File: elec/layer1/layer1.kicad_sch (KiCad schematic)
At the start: 124 parts, among them J1 XT30PW-M, J2 XT30PW-M, J3 Conn_01x04, J4 XT30PW-M, J5 XT30PW-M, SW2 SW_SPDT_312, U1 CD74HC4067SM, U2 CD74HC4067SM, U3 TEENSY40

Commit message: fix: l1 gnd
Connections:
- net GND: now also U3.G1, U3.G2, U3.G3
- no-connect marks 24 -> 21
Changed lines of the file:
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@@
 	(title_block
 		(title "Robocup 2026 Layer 1")
-		(date "2026-01-28")
-		(rev "0.1")
+		(date "2026-01-29")
+		(rev "1.0")
 		(company "Vent Exhaust")
 		(comment 1 "Ng Chen-Xuan")
@@
 	)
 	(no_connect
-		(at 247.65 170.18)
-	)
-	(no_connect
 		(at 247.65 198.12)
 	)
@@
 	)
 	(no_connect
-		(at 283.21 172.72)
-	)
-	(no_connect
 		(at 283.21 175.26)
 	)
@@
 	)
 	(no_connect
-		(at 247.65 213.36)
-	)
-	(no_connect
 		(at 283.21 180.34)
 	)
@@
 	(wire
 		(pts
+			(xy 234.95 170.18) (xy 247.65 170.18)
+		)
+		(stroke
+			(width 0)
+			(type default)
+		)
+	)
+	(wire
+		(pts
 			(xy 57.15 208.28) (xy 57.15 207.01)
 		)
@@
 	(wire
 		(pts
+			(xy 234.95 213.36) (xy 247.65 213.36)
+		)
+		(stroke
+			(width 0)
+			(type default)
+		)
+	)
+	(wire
+		(pts
 			(xy 146.05 31.75) (xy 146.05 33.02)
 		)
@@
 	(wire
 		(pts
+			(xy 283.21 172.72) (xy 295.91 172.72)
+		)
+		(stroke
+			(width 0)
+			(type default)
+		)
+	)
+	(wire
+		(pts
 			(xy 176.53 190.5) (xy 176.53 189.23)
 		)
@@
 	)
 	(symbol
+		(lib_id "power:GND")
+		(at 234.95 170.18 270)
+		(unit 1)
+		(exclude_from_sim no)
+		(in_bom yes)
+		(on_board yes)
+		(dnp no)
+		(fields_autoplaced yes)
+		(property "Reference" "#PWR039"
+			(at 228.6 170.18 0)
+			(effects
+				(font
+					(size 1.27 1.27)
+				)
+				(hide yes)
+			)
+		)
+		(property "Value" "GND"
+			(at 231.14 170.1799 90)
+			(effects
+				(font
+					(size 1.27 1.27)
+				)
+				(justify right)
+			)
+		)
+		(property "Footprint" ""
+			(at 234.95 170.18 0)
+			(effects
+				(font
+					(size 1.27 1.27)
+				)
+				(hide yes)
+			)
+		)
+		(property "Datasheet" ""
+			(at 234.95 170.18 0)
+			(effects
+				(font
+					(size 1.27 1.27)
+				)
+				(hide yes)
+			)
+		)
+		(property "Description" "Power symbol creates a global label with name \"GND\" , ground"
+			(at 234.95 170.18 0)
+			(effects
+				(font
+					(size 1.27 1.27)
+				)
+				(hide yes)
+			)
+		)
+		(pin "1"
+		)
+		(instances
+			(project "layer1"
+				(path "/65f958e3-40ee-4841-b9d1-28823b8d4e62"
+					(reference "#PWR039")
+					(unit 1)
+				)
+			)
+		)
+	)
+	(symbol
 		(lib_id "power:+3V3")
 		(at 135.89 246.38 0)
@@
 	)
 	(symbol
+		(lib_id "power:GND")
+		(at 295.91 172.72 90)
+		(unit 1)
+		(exclude_from_sim no)
+		(in_bom yes)
+		(on_board yes)
+		(dnp no)
+		(fields_autoplaced yes)
+		(property "Reference" "#PWR038"
+			(at 302.26 172.72 0)
+			(effects
+				(font
+					(size 1.27 1.27)
+				)
+				(hide yes)
+			)
+		)
+		(property "Value" "GND"
+			(at 299.72 172.7199 90)
+			(effects
+				(font
+					(size 1.27 1.27)
+				)
+				(justify right)
+			)
+		)
+		(property "Footprint" ""
+			(at 295.91 172.72 0)
+			(effects
+				(font
+					(size 1.27 1.27)
+				)
+				(hide yes)
+			)
+		)
+		(property "Datasheet" ""
+			(at 295.91 172.72 0)
+			(effects
+				(font
+					(size 1.27 1.27)
+				)
+				(hide yes)
+			)
+		)
+		(property "Description" "Power symbol creates a global label with name \"GND\" , ground"
+			(at 295.91 172.72 0)
+			(effects
+				(font
+					(size 1.27 1.27)
+				)
+				(hide yes)
+			)
+		)
+		(pin "1"
+		)
+		(instances
+			(project ""
+				(path "/65f958e3-40ee-4841-b9d1-28823b8d4e62"
+					(reference "#PWR038")
+					(unit 1)
+				)
+			)
+		)
+	)
+	(symbol
 		(lib_id "Device:LED")
 		(at 259.08 36.83 90)
@@
 					(unit 1)
 				)
+			)
+		)
+	)
+	(symbol
+		(lib_id "power:GND")
+		(at 234.95 213.36 270)
+		(unit 1)
+		(exclude_from_sim no)
+		(in_bom yes)
+		(on_board yes)
+		(dnp no)
+		(fields_autoplaced yes)
+		(property "Reference" "#PWR040"
+			(at 228.6 213.36 0)
+			(effects
+				(font
+					(size 1.27 1.27)
+				)
+				(hide yes)
+			)
+		)
+		(property "Value" "GND"
+			(at 231.14 213.3599 90)
+			(effects
+				(font
+					(size 1.27 1.27)
+				)
+				(justify right)
+			)
+		)
+		(property "Footprint" ""
+			(at 234.95 213.36 0)
+			(effects
+				(font
+					(size 1.27 1.27)
+				)
+				(hide yes)
+			)
+		)
+		(property "Datasheet" ""
+			(at 234.95 213.36 0)
+			(effects
+				(font
+					(size 1.27 1.27)
+				)
+				(hide yes)
+			)
+		)
+		(property "Description" "Power symbol creates a global label with name \"GND\" , ground"
+			(at 234.95 213.36 0)
+			(effects
+				(font
+					(size 1.27 1.27)
+				)
+				(hide yes)
+			)
+		)
+		(pin "1"
+		)
+		(instances
+			(project "layer1"
+				(path "/65f958e3-40ee-4841-b9d1-28823b8d4e62"
+					(reference "#PWR040")
+					(unit 1)
+				)

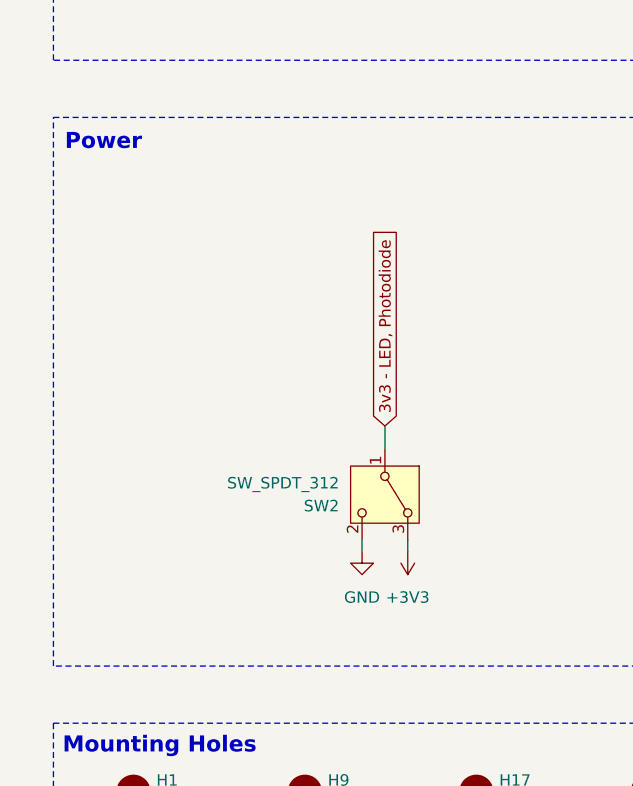
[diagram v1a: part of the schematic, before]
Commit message: changed chenxuan mistake on l1
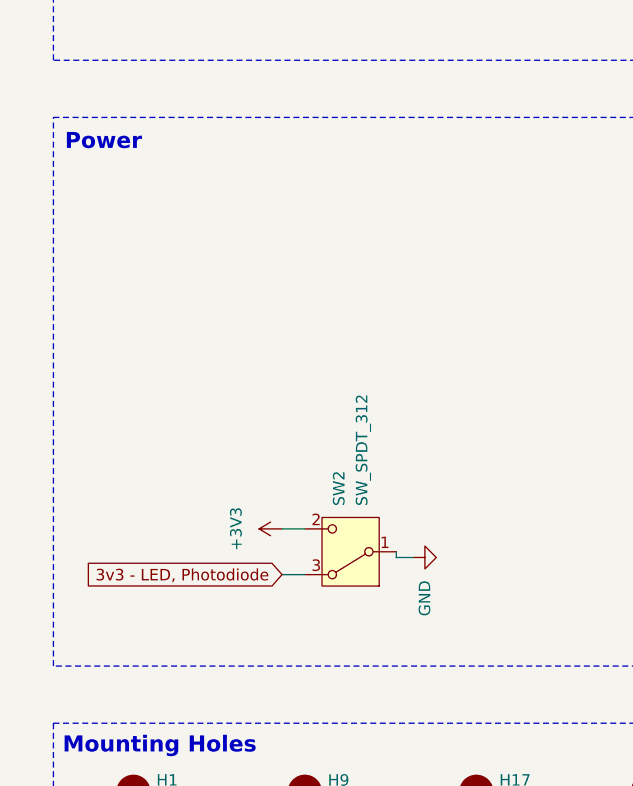
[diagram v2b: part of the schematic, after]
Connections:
- net +3V3: now also SW2.2 (C); no longer SW2.3 (A)
- net 3v3 - LED, Photodiode: now also SW2.3 (A); no longer SW2.1 (B)
- net GND: now also SW2.1 (B); no longer SW2.2 (C)
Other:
- moved on the sheet: SW2
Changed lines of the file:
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@@
 	(wire
 		(pts
+			(xy 55.88 208.915) (xy 57.785 208.915)
+		)
+		(stroke
+			(width 0)
+			(type default)
+		)
+	)
+	(wire
+		(pts
 			(xy 170.18 87.63) (xy 172.72 87.63)
 		)
@@
 	(wire
 		(pts
+			(xy 43.18 210.82) (xy 45.72 210.82)
+		)
+		(stroke
+			(width 0)
+			(type default)
+		)
+	)
+	(wire
+		(pts
 			(xy 95.25 31.75) (xy 105.41 31.75)
 		)
@@
 	(wire
 		(pts
-			(xy 57.15 208.28) (xy 57.15 207.01)
-		)
-		(stroke
-			(width 0)
-			(type default)
-		)
-	)
-	(wire
-		(pts
 			(xy 81.28 87.63) (xy 83.82 87.63)
 		)
@@
 	(wire
 		(pts
+			(xy 43.18 205.74) (xy 45.72 205.74)
+		)
+		(stroke
+			(width 0)
+			(type default)
+		)
+	)
+	(wire
+		(pts
 			(xy 135.89 40.64) (xy 135.89 41.91)
 		)
@@
 	(wire
 		(pts
+			(xy 55.88 208.28) (xy 55.88 208.915)
+		)
+		(stroke
+			(width 0)
+			(type default)
+		)
+	)
+	(wire
+		(pts
 			(xy 340.36 41.91) (xy 330.2 41.91)
 		)
@@
 	(wire
 		(pts
-			(xy 54.61 194.31) (xy 54.61 196.85)
-		)
-		(stroke
-			(width 0)
-			(type default)
-		)
-	)
-	(wire
-		(pts
 			(xy 160.02 123.19) (xy 160.02 124.46)
 		)
@@
 	(wire
 		(pts
-			(xy 52.07 208.28) (xy 52.07 207.01)
-		)
-		(stroke
-			(width 0)
-			(type default)
-		)
-	)
-	(wire
-		(pts
 			(xy 185.42 187.96) (xy 185.42 189.23)
 		)
@@
 	(global_label "3v3 - LED, Photodiode"
 		(shape input)
-		(at 54.61 194.31 90)
+		(at 43.18 210.82 180)
 		(fields_autoplaced yes)
 		(effects
@@
 				(size 1.27 1.27)
 			)
-			(justify left)
+			(justify right)
 		)
 		(property "Intersheetrefs" "${INTERSHEET_REFS}"
-			(at 54.61 168.828 90)
+			(at 17.698 210.82 0)
 			(effects
 				(font
 					(size 1.27 1.27)
 				)
-				(justify left)
+				(justify right)
 				(hide yes)
 			)
@@
 	(symbol
 		(lib_id "power:GND")
-		(at 52.07 208.28 0)
+		(at 57.785 208.915 90)
 		(unit 1)
 		(exclude_from_sim no)
@@
 		(fields_autoplaced yes)
 		(property "Reference" "#PWR027"
-			(at 52.07 214.63 0)
+			(at 64.135 208.915 0)
 			(effects
 				(font
@@
 		)
 		(property "Value" "GND"
-			(at 52.07 213.36 0)
+			(at 59.0551 211.455 0)
 			(effects
 				(font
 					(size 1.27 1.27)
 				)
+				(justify right)
 			)
 		)
 		(property "Footprint" ""
-			(at 52.07 208.28 0)
+			(at 57.785 208.915 0)
 			(effects
 				(font
@@
 		)
 		(property "Datasheet" ""
-			(at 52.07 208.28 0)
+			(at 57.785 208.915 0)
 			(effects
 				(font
@@
 		)
 		(property "Description" "Power symbol creates a global label with name \"GND\" , ground"
-			(at 52.07 208.28 0)
+			(at 57.785 208.915 0)
 			(effects
 				(font
@@
 	(symbol
 		(lib_id "Switch:SW_SPDT_312")
-		(at 54.61 201.93 270)
+		(at 50.8 208.28 180)
 		(unit 1)
 		(exclude_from_sim no)
@@
 		(fields_autoplaced yes)
 		(property "Reference" "SW2"
-			(at 49.53 203.2001 90)
+			(at 49.5299 203.2 90)
 			(effects
 				(font
@@
 		)
 		(property "Value" "SW_SPDT_312"
-			(at 49.53 200.6601 90)
+			(at 52.0699 203.2 90)
 			(effects
 				(font
@@
 		)
 		(property "Footprint" "layer1-pcb-footprints:SS12D00G3"
-			(at 44.45 201.93 0)
+			(at 50.8 198.12 0)
 			(effects
 				(font
@@
 		)
 		(property "Datasheet" "~"
-			(at 46.99 201.93 0)
+			(at 50.8 200.66 0)
 			(effects
 				(font
@@
 		)
 		(property "Description" "Switch, single pole double throw"
-			(at 54.61 201.93 0)
+			(at 50.8 208.28 0)
 			(effects
 				(font
@@
 	(symbol
 		(lib_id "power:+3V3")
-		(at 57.15 208.28 180)
+		(at 43.18 205.74 90)
 		(unit 1)
 		(exclude_from_sim no)
@@
 		(fields_autoplaced yes)
 		(property "Reference" "#PWR01"
-			(at 57.15 204.47 0)
+			(at 46.99 205.74 0)
 			(effects
 				(font
@@
 		)
 		(property "Value" "+3V3"
-			(at 57.15 213.36 0)
+			(at 38.1 205.74 0)
 			(effects
 				(font
@@
 		)
 		(property "Footprint" ""
-			(at 57.15 208.28 0)
+			(at 43.18 205.74 0)
 			(effects
 				(font
@@
 		)
 		(property "Datasheet" ""
-			(at 57.15 208.28 0)
+			(at 43.18 205.74 0)
 			(effects
 				(font
@@
 		)
 		(property "Description" "Power symbol creates a global label with name \"+3V3\""
-			(at 57.15 208.28 0)
+			(at 43.18 205.74 0)
 			(effects
 				(font

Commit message: did l1 add res partially
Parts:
- added C5, C6: 220u, Capacitor_Tantalum_SMD:CP_EIA-7343-15_Kemet-W_HandSolder, symbol Device:C_Polarized
- added R10, R11, R12, R13, R14, R15, R16, R17, R18, R19, R20, R21, R22, R23, R24, R25, R26, R27, R28, R29, R30, R31, R32, R33, R34, R35, R36, R5, R6, R7, R8, R9: 0R39, Resistor_SMD:R_0603_1608Metric, symbol Device:R
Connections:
- net +3V3: now also C5.1, C6.1
- net 3v3 - LED, Photodiode: now also R10.1, R11.1, R12.1, R13.1, R14.1, R15.1, R16.1, R17.1, R18.1, R19.1, R20.1, R21.1, R22.1, R23.1, R24.1, R25.1, R26.1, R27.1, R28.1, R29.1, R30.1, R31.1, R32.1, R33.1, R34.1, R35.1, R36.1, R5.1, R6.1, R7.1, R8.1, R9.1; no longer D1.2 (A), D10.2 (A), D11.2 (A), D12.2 (A), D13.2 (A), D14.2 (A), D15.2 (A), D16.2 (A), D17.2 (A), D18.2 (A), D19.2 (A), D2.2 (A), D20.2 (A), D21.2 (A), D22.2 (A), D23.2 (A), D24.2 (A), D25.2 (A), D26.2 (A), D27.2 (A), D28.2 (A), D29.2 (A), D3.2 (A), D30.2 (A), D31.2 (A), D32.2 (A), D4.2 (A), D5.2 (A), D6.2 (A), D7.2 (A), D8.2 (A), D9.2 (A)
- net GND: now also C5.2, C6.2
- new net: D30.2 (A), R34.2
- new net: D14.2 (A), R18.2
- new net: D29.2 (A), R33.2
- new net: D12.2 (A), R16.2
- new net: D17.2 (A), R21.2
- new net: D13.2 (A), R17.2
- new net: D26.2 (A), R30.2
- new net: D10.2 (A), R14.2
- new net: D23.2 (A), R27.2
- new net: D5.2 (A), R9.2
- new net: D19.2 (A), R23.2
- new net: D20.2 (A), R24.2
- new net: D15.2 (A), R19.2
- new net: D9.2 (A), R13.2
- new net: D24.2 (A), R28.2
- new net: D7.2 (A), R11.2
- new net: D1.2 (A), R5.2
- new net: D8.2 (A), R12.2
- new net: D3.2 (A), R7.2
- new net: D4.2 (A), R8.2
- new net: D21.2 (A), R25.2
- new net: D18.2 (A), R22.2
- new net: D22.2 (A), R26.2
- new net: D32.2 (A), R36.2
- new net: D31.2 (A), R35.2
- new net: D6.2 (A), R10.2
- new net: D16.2 (A), R20.2
- new net: D25.2 (A), R29.2
- new net: D2.2 (A), R6.2
- new net: D11.2 (A), R15.2
- new net: D27.2 (A), R31.2
- new net: D28.2 (A), R32.2
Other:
- moved on the sheet: D1, D10, D11, D12, D13, D14, D15, D16, D17, D18, D19, D2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

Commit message: fix: l1; prod: l1
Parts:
- H1, H2: footprint MountingHole:MountingHole_2.2mm_M2_DIN965_Pad_TopBottom -> MountingHole:MountingHole_3.2mm_M3_DIN965_Pad_TopBottom
- R10, R11, R12, R13, R14, R15, R16, R17, R18, R19, R20, R21, R22, R23, R24, R25, R26, R27, R28, R29, R30, R31, R32, R33, R34, R35, R36, R5, R6, R7, R8, R9: value 0R39 -> 10R
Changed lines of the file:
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@@
 	(wire
 		(pts
-			(xy 43.18 27.94) (xy 76.2 27.94)
+			(xy 63.5 27.94) (xy 76.2 27.94)
 		)
 		(stroke
@@
 	(wire
 		(pts
-			(xy 43.18 27.94) (xy 43.18 25.4)
-		)
-		(stroke
-			(width 0)
-			(type default)
-		)
-	)
-	(wire
-		(pts
 			(xy 60.96 96.52) (xy 60.96 97.79)
 		)
@@
 	(global_label "3v3 - LED, Photodiode"
 		(shape input)
-		(at 43.18 25.4 180)
+		(at 63.5 27.94 180)
 		(fields_autoplaced yes)
 		(effects
@@
 		)
 		(property "Intersheetrefs" "${INTERSHEET_REFS}"
-			(at 17.698 25.4 0)
+			(at 38.018 27.94 0)
 			(effects
 				(font
@@
 			)
 		)
-		(property "Value" "0R39"
+		(property "Value" "10R"
 			(at 374.65 34.2899 0)
 			(effects
@@
 			)
 		)
-		(property "Value" "0R39"
+		(property "Value" "10R"
 			(at 210.82 34.2899 0)
 			(effects
@@
 			)
 		)
-		(property "Value" "0R39"
+		(property "Value" "10R"
 			(at 334.01 34.2899 0)
 			(effects
@@
 			)
 		)
-		(property "Value" "0R39"
+		(property "Value" "10R"
 			(at 190.5 34.2899 0)
 			(effects
@@
 			)
 		)
-		(property "Value" "0R39"
+		(property "Value" "10R"
 			(at 170.18 34.2899 0)
 			(effects
@@
 			)
 		)
-		(property "Value" "0R39"
+		(property "Value" "10R"
 			(at 303.53 34.2899 0)
 			(effects
@@
 			)
 		)
-		(property "Value" "0R39"
+		(property "Value" "10R"
 			(at 119.38 34.2899 0)
 			(effects
@@
 			)
 		)
-		(property "Value" "0R39"
+		(property "Value" "10R"
 			(at 200.66 34.2899 0)
 			(effects
@@
 			)
 		)
-		(property "Value" "0R39"
+		(property "Value" "10R"
 			(at 364.49 34.2899 0)
 			(effects
@@
 			)
 		)
-		(property "Value" "0R39"
+		(property "Value" "10R"
 			(at 220.98 34.2899 0)
 			(effects
@@
 			)
 		)
-		(property "Footprint" "MountingHole:MountingHole_2.2mm_M2_DIN965_Pad_TopBottom"
+		(property "Footprint" "MountingHole:MountingHole_3.2mm_M3_DIN965_Pad_TopBottom"
 			(at 26.67 240.03 0)
 			(effects
@@
 			)
 		)
-		(property "Value" "0R39"
+		(property "Value" "10R"
 			(at 313.69 34.2899 0)
 			(effects
@@
 			)
 		)
-		(property "Value" "0R39"
+		(property "Value" "10R"
 			(at 139.7 34.2899 0)
 			(effects
@@
 			)
 		)
-		(property "Footprint" "MountingHole:MountingHole_2.2mm_M2_DIN965_Pad_TopBottom"
+		(property "Footprint" "MountingHole:MountingHole_3.2mm_M3_DIN965_Pad_TopBottom"
 			(at 26.67 234.95 0)
 			(effects
@@
 			)
 		)
-		(property "Value" "0R39"
+		(property "Value" "10R"
 			(at 109.22 34.2899 0)
 			(effects
@@
 			)
 		)
-		(property "Value" "0R39"
+		(property "Value" "10R"
 			(at 252.73 34.2899 0)
 			(effects
@@
 			)
 		)
-		(property "Value" "0R39"
+		(property "Value" "10R"
 			(at 149.86 34.2899 0)
 			(effects
@@
 			)
 		)
-		(property "Value" "0R39"
+		(property "Value" "10R"
 			(at 99.06 34.2899 0)
 			(effects
@@
 			)
 		)
-		(property "Value" "0R39"
+		(property "Value" "10R"
 			(at 384.81 34.2899 0)
 			(effects
@@
 			)
 		)
-		(property "Value" "0R39"
+		(property "Value" "10R"
 			(at 129.54 34.2899 0)
 			(effects
@@
 			)
 		)
-		(property "Value" "0R39"
+		(property "Value" "10R"
 			(at 262.89 34.2899 0)
 			(effects
@@
 			)
 		)
-		(property "Value" "0R39"
+		(property "Value" "10R"
 			(at 160.02 34.2899 0)
 			(effects
@@
 			)
 		)
-		(property "Value" "0R39"
+		(property "Value" "10R"
 			(at 283.21 34.2899 0)
 			(effects
@@
 			)
 		)
-		(property "Value" "0R39"
+		(property "Value" "10R"
 			(at 231.14 34.2899 0)
 			(effects
@@
 			)
 		)
-		(property "Value" "0R39"
+		(property "Value" "10R"
 			(at 394.97 34.2899 0)
 			(effects
@@
 			)
 		)
-		(property "Value" "0R39"
+		(property "Value" "10R"
 			(at 323.85 34.2899 0)
 			(effects
@@
 			)
 		)
-		(property "Value" "0R39"
+		(property "Value" "10R"
 			(at 242.57 34.2899 0)
 			(effects
@@
 			)
 		)
-		(property "Value" "0R39"
+		(property "Value" "10R"
 			(at 88.9 34.2899 0)
 			(effects
@@
 			)
 		)
-		(property "Value" "0R39"
+		(property "Value" "10R"
 			(at 78.74 34.2899 0)
 			(effects
@@
 			)
 		)
-		(property "Value" "0R39"
+		(property "Value" "10R"
 			(at 293.37 34.2899 0)
 			(effects
@@
 			)
 		)
-		(property "Value" "0R39"
+		(property "Value" "10R"
 			(at 273.05 34.2899 0)
 			(effects
@@
 			)
 		)
-		(property "Value" "0R39"
+		(property "Value" "10R"
 			(at 180.34 34.2899 0)
 			(effects
@@
 			)
 		)
-		(property "Value" "0R39"
+		(property "Value" "10R"
 			(at 354.33 34.2899 0)
 			(effects
@@
 			)
 		)
-		(property "Value" "0R39"
+		(property "Value" "10R"
 			(at 344.17 34.2899 0)
 			(effects
